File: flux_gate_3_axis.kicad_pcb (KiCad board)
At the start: 4 copper layers, 44 x 51.1 mm, 60 parts, among them J1 Conn_02x04_Odd_Even, J2 Conn_02x04_Odd_Even, J3 Conn_02x04_Odd_Even, J4 Conn_01x02, J5 Conn_01x02, J6 Conn_02x04_Odd_Even, J7 Conn_01x02, U1 Pico, U2 DRV425, U3 DRV425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

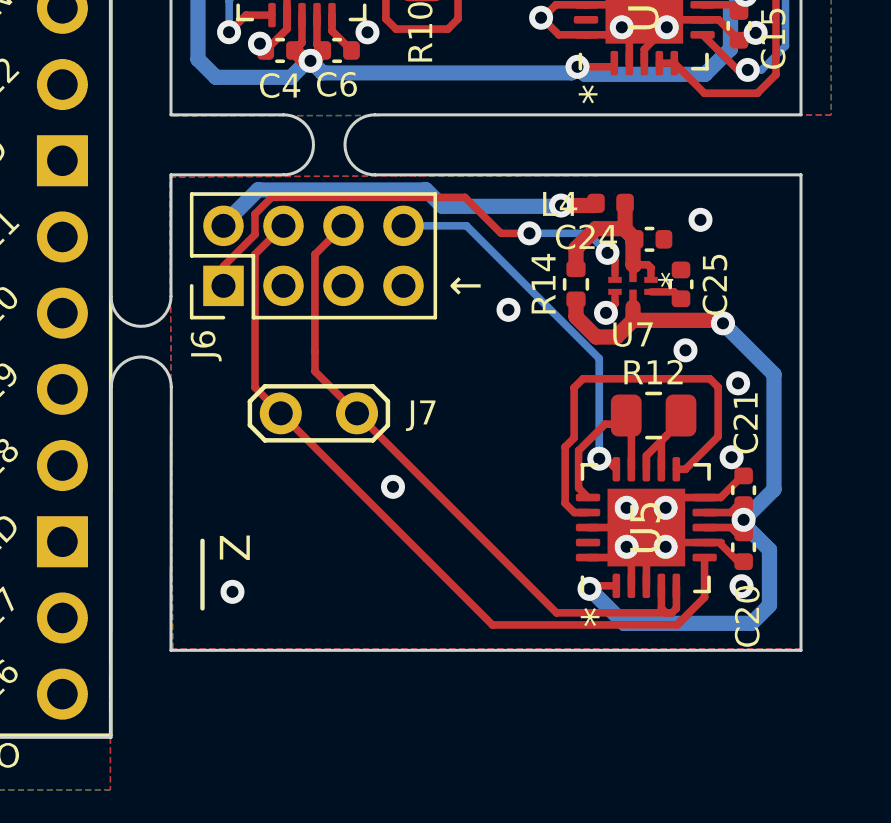
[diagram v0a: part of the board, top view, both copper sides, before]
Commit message: improved ground connectivity
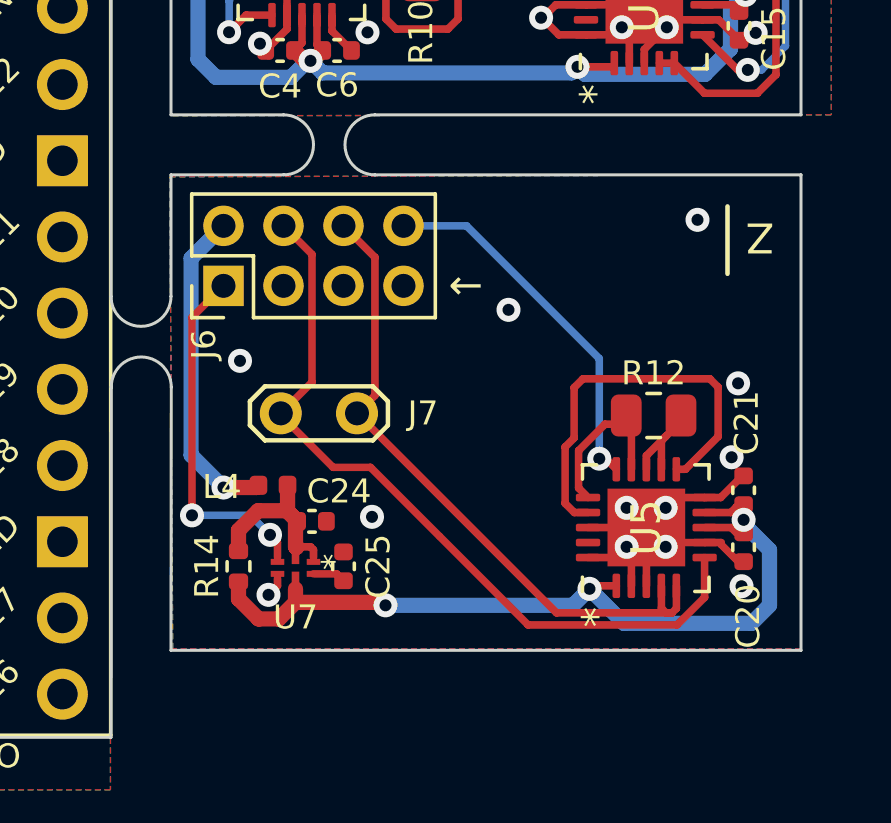
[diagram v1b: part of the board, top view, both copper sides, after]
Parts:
- moved C24 14.7 mm to (42.5, 59.1)
- moved C25 14.7 mm to (43.5, 60.6)
- moved L4 14.7 mm to (41.2, 57.9)
- moved R14 14.7 mm to (40.0, 60.6)
- moved U7 14.7 mm to (42.0, 60.6)
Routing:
- net DRV_ON: track 114.0 -> 109.4 mm
- net VDC: track 125.6 -> 123.3 mm
- net VDRV2: track 28.3 -> 27.7 mm
- net GND: vias 40 -> 39
